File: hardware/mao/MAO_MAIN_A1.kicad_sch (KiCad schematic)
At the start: 0 parts

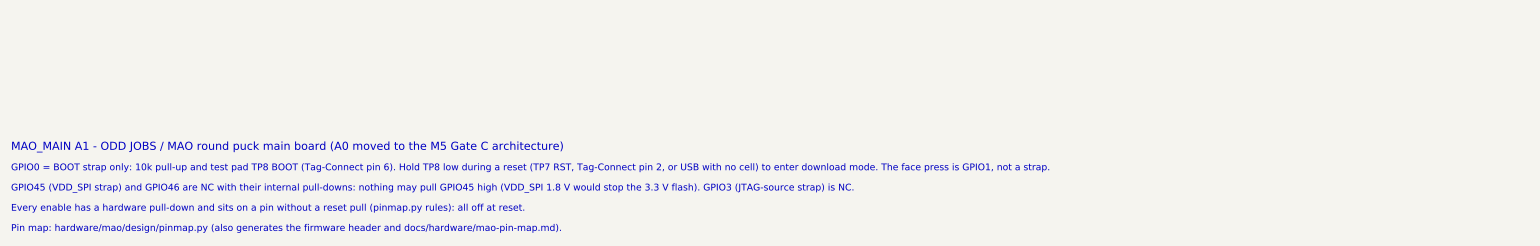
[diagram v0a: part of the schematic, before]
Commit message: A1 capture/layout follow the pin swaps (ERC 0); escapes and fixture pads moved with their nets
Co-Authored-By: Claude Opus 5.5 <noreply@anthropic.com>
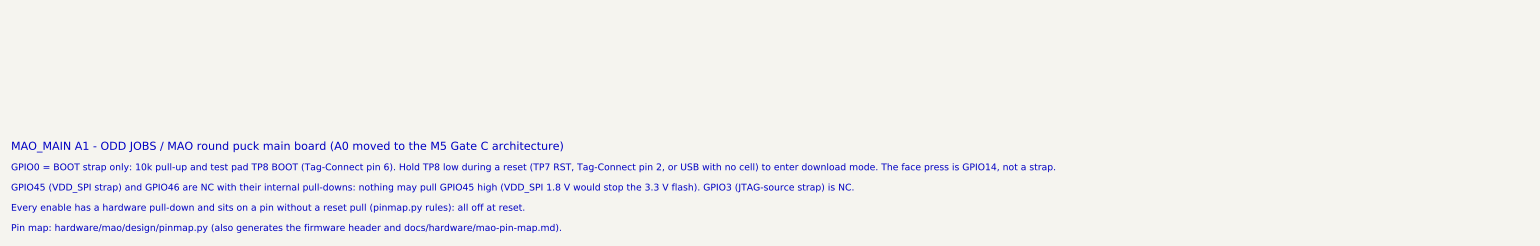
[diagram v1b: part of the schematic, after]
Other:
- note added: "GPIO0 = BOOT strap only: 10k pull-up and test pad TP8 BOOT (Tag-Connect pin 6). Hold TP8 low during a reset (TP7 RST, Tag-Connect pin 2, or USB with no cell) to enter download mode. The face press is GPIO14, not a strap."
- note removed: "GPIO0 = BOOT strap only: 10k pull-up and test pad TP8 BOOT (Tag-Connect pin 6). Hold TP8 low during a reset (TP7 RST, Tag-Connect pin 2, or USB with no cell) to enter download mode. The face press is GPIO1, not a strap."
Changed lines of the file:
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@@
 		)
 	)
-	(text "GPIO0 = BOOT strap only: 10k pull-up and test pad TP8 BOOT (Tag-Connect pin 6). Hold TP8 low during a reset (TP7 RST, Tag-Connect pin 2, or USB with no cell) to enter download mode. The face press is GPIO1, not a strap."
+	(text "GPIO0 = BOOT strap only: 10k pull-up and test pad TP8 BOOT (Tag-Connect pin 6). Hold TP8 low during a reset (TP7 RST, Tag-Connect pin 2, or USB with no cell) to enter download mode. The face press is GPIO14, not a strap."
 		(exclude_from_sim no)
 		(at 25.4 219.71 0)
